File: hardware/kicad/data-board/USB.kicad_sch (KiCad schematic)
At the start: 33 parts, among them J14 Conn_02x05_Odd_Even, J5 USB_67298-4090, J7 USB_OTG, U13 FSUSB42MUX, U6 USB2514B_Bi, U7 AP2553W6, Y1 24MHz

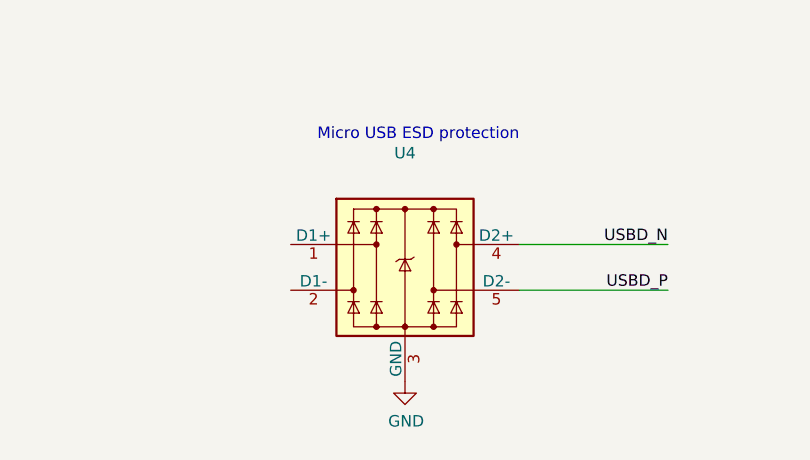
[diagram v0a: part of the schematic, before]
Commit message: breaks out PoE ttap
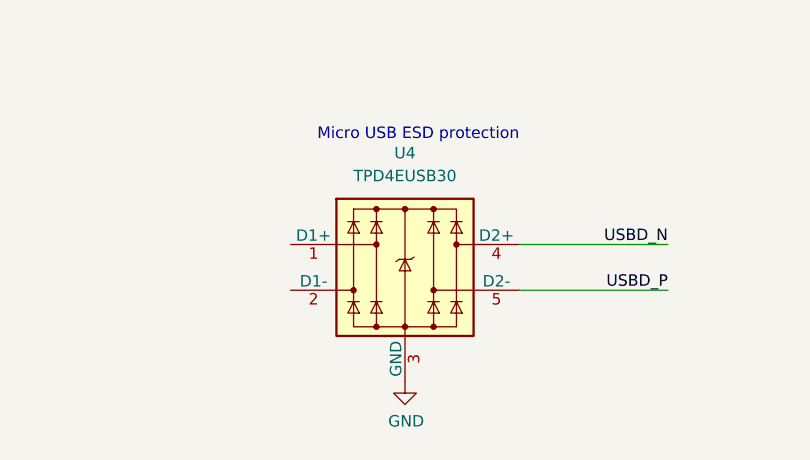
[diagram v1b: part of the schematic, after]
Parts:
- U4: value (none) -> TPD4EUSB30; footprint (none) -> Package_SON:USON-10_2.5x1.0mm_P0.5mm
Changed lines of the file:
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@@
     (in_bom yes) (on_board yes) (fields_autoplaced)
     (property "Reference" "U4" (id 0) (at 323.85 80.01 0))
-    (property "Value" "" (id 1) (at 323.85 82.55 0))
-    (property "Footprint" "" (id 2) (at 299.72 102.87 0)
+    (property "Value" "TPD4EUSB30" (id 1) (at 323.85 82.55 0))
+    (property "Footprint" "Package_SON:USON-10_2.5x1.0mm_P0.5mm" (id 2) (at 299.72 102.87 0)
       (effects (font (size 1.27 1.27)) hide)
     )
